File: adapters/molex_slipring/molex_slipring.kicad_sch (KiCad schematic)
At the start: 3 parts, among them J1 RJ45 RJE591885401, J2 5055680571

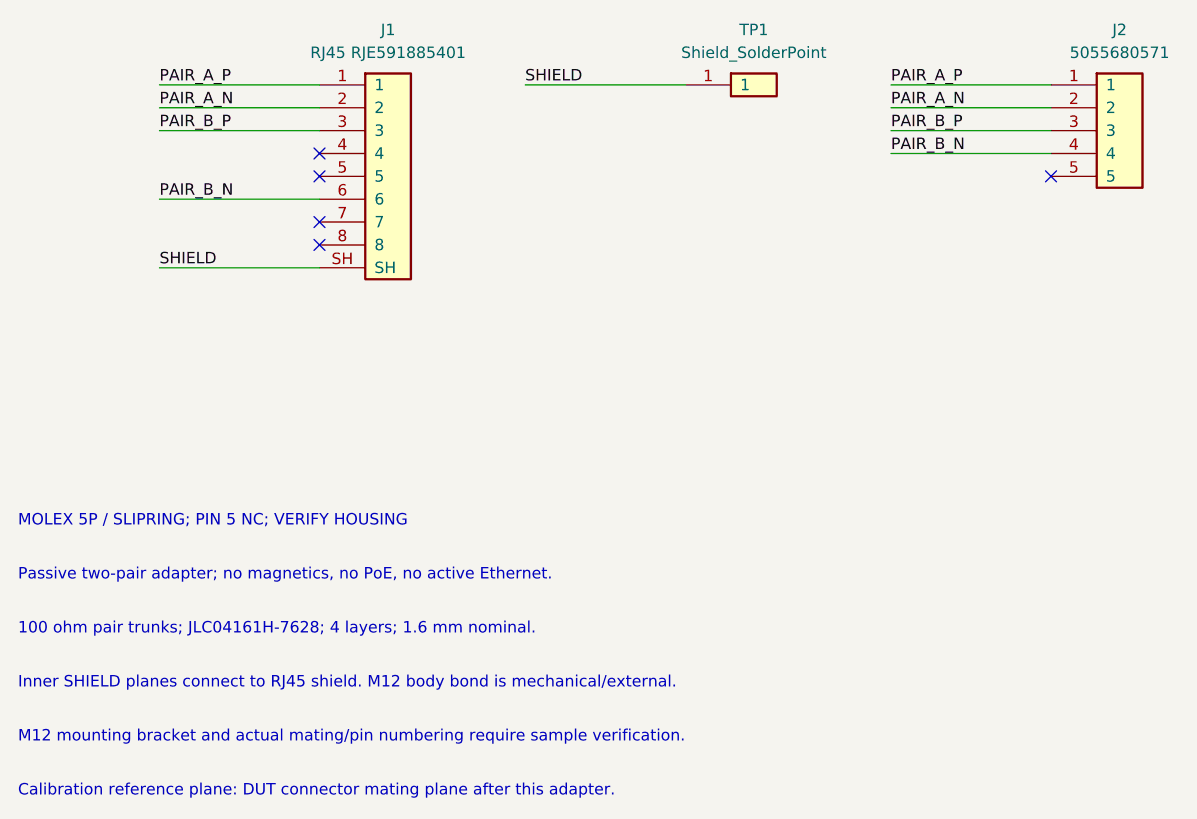
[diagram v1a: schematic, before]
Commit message: Refine Molex slip-ring adapter routing
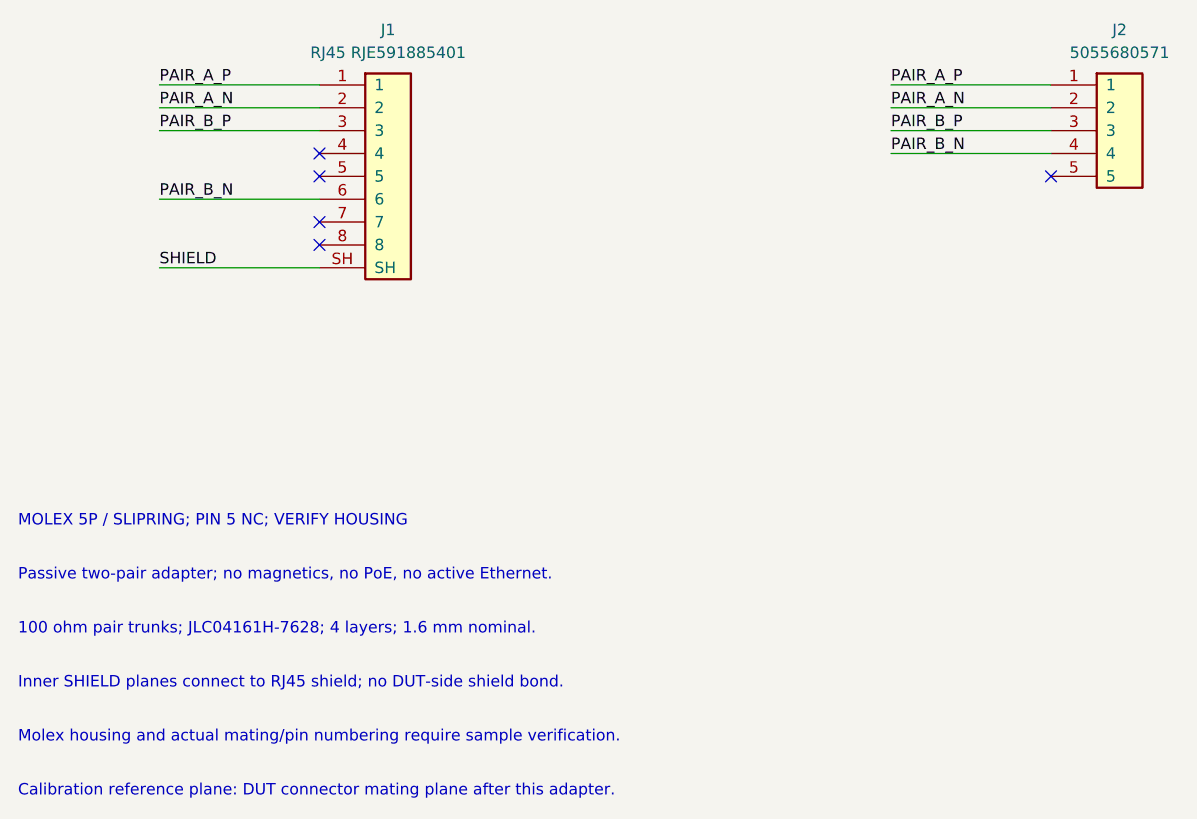
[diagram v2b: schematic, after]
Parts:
- removed TP1: Shield_SolderPoint, adapter:Shield_SolderPoint, symbol Adapter:Shield
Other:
- note added: "Inner SHIELD planes connect to RJ45 shield; no DUT-side shield bond."
- note added: "Molex housing and actual mating/pin numbering require sample verification."
- note removed: "Inner SHIELD planes connect to RJ45 shield. M12 body bond is mechanical/external."
- note removed: "M12 mounting bracket and actual mating/pin numbering require sample verification."
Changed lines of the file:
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@@
 (label "PAIR_B_N" (at 127.0 71.12 0) (effects (font (size 1.27 1.27)) (justify left bottom)))
 (no_connect (at 144.78 73.66))
-(symbol (lib_id "Adapter:Shield") (at 111.76 63.5 0) (unit 1) (in_bom no) (on_board yes) (dnp no)
-          (property "Reference" "TP1" (at 111.76 57.38 0) (effects (font (size 1.27 1.27))))
-          (property "Value" "Shield_SolderPoint" (at 111.76 59.92 0) (effects (font (size 1.27 1.27))))
-          (property "Footprint" "adapter:Shield_SolderPoint" (at 111.76 65 0) (effects (font (size 1.27 1.27)) (hide yes)))
-          (property "Datasheet" "" (at 111.76 65 0) (effects (font (size 1.27 1.27)) (hide yes)))
-          (property "Description" "" (at 111.76 65 0) (effects (font (size 1.27 1.27)) (hide yes)))
-          (instances (project "molex_slipring" (path "/5e6f90af-e298-5171-be59-d794e5e80902" (reference "TP1") (unit 1)))))
-(wire (pts (xy 104.14 63.5) (xy 86.36000000000001 63.5)) (stroke (width 0) (type default)))
-(label "SHIELD" (at 86.36000000000001 63.5 0) (effects (font (size 1.27 1.27)) (justify left bottom)))
 (text "MOLEX 5P / SLIPRING; PIN 5 NC; VERIFY HOUSING" (at 30 112 0) (effects (font (size 1.27 1.27)) (justify left)))
 (text "Passive two-pair adapter; no magnetics, no PoE, no active Ethernet." (at 30 118 0) (effects (font (size 1.27 1.27)) (justify left)))
 (text "100 ohm pair trunks; JLC04161H-7628; 4 layers; 1.6 mm nominal." (at 30 124 0) (effects (font (size 1.27 1.27)) (justify left)))
-(text "Inner SHIELD planes connect to RJ45 shield. M12 body bond is mechanical/external." (at 30 130 0) (effects (font (size 1.27 1.27)) (justify left)))
-(text "M12 mounting bracket and actual mating/pin numbering require sample verification." (at 30 136 0) (effects (font (size 1.27 1.27)) (justify left)))
+(text "Inner SHIELD planes connect to RJ45 shield; no DUT-side shield bond." (at 30 130 0) (effects (font (size 1.27 1.27)) (justify left)))
+(text "Molex housing and actual mating/pin numbering require sample verification." (at 30 136 0) (effects (font (size 1.27 1.27)) (justify left)))
 (text "Calibration reference plane: DUT connector mating plane after this adapter." (at 30 142 0) (effects (font (size 1.27 1.27)) (justify left)))
       (sheet_instances (path "/" (page "1"))) (embedded_fonts no))
